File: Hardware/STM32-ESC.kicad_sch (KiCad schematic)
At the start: 0 parts

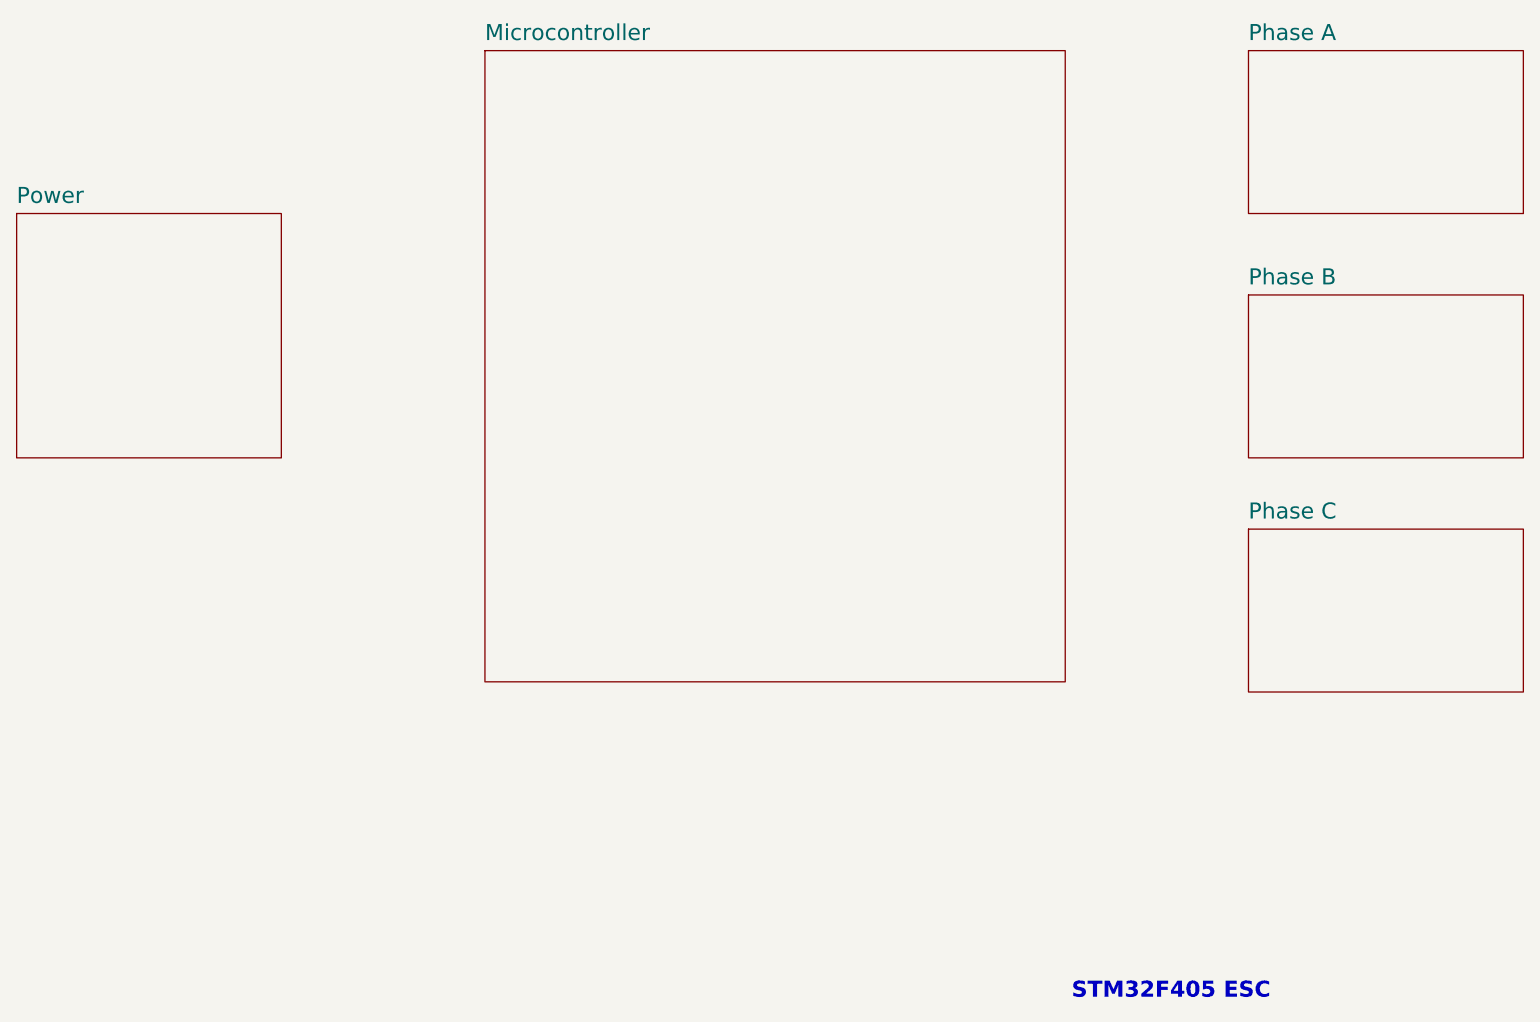
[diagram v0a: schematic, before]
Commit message: feat: Update to use I2C stemma connector
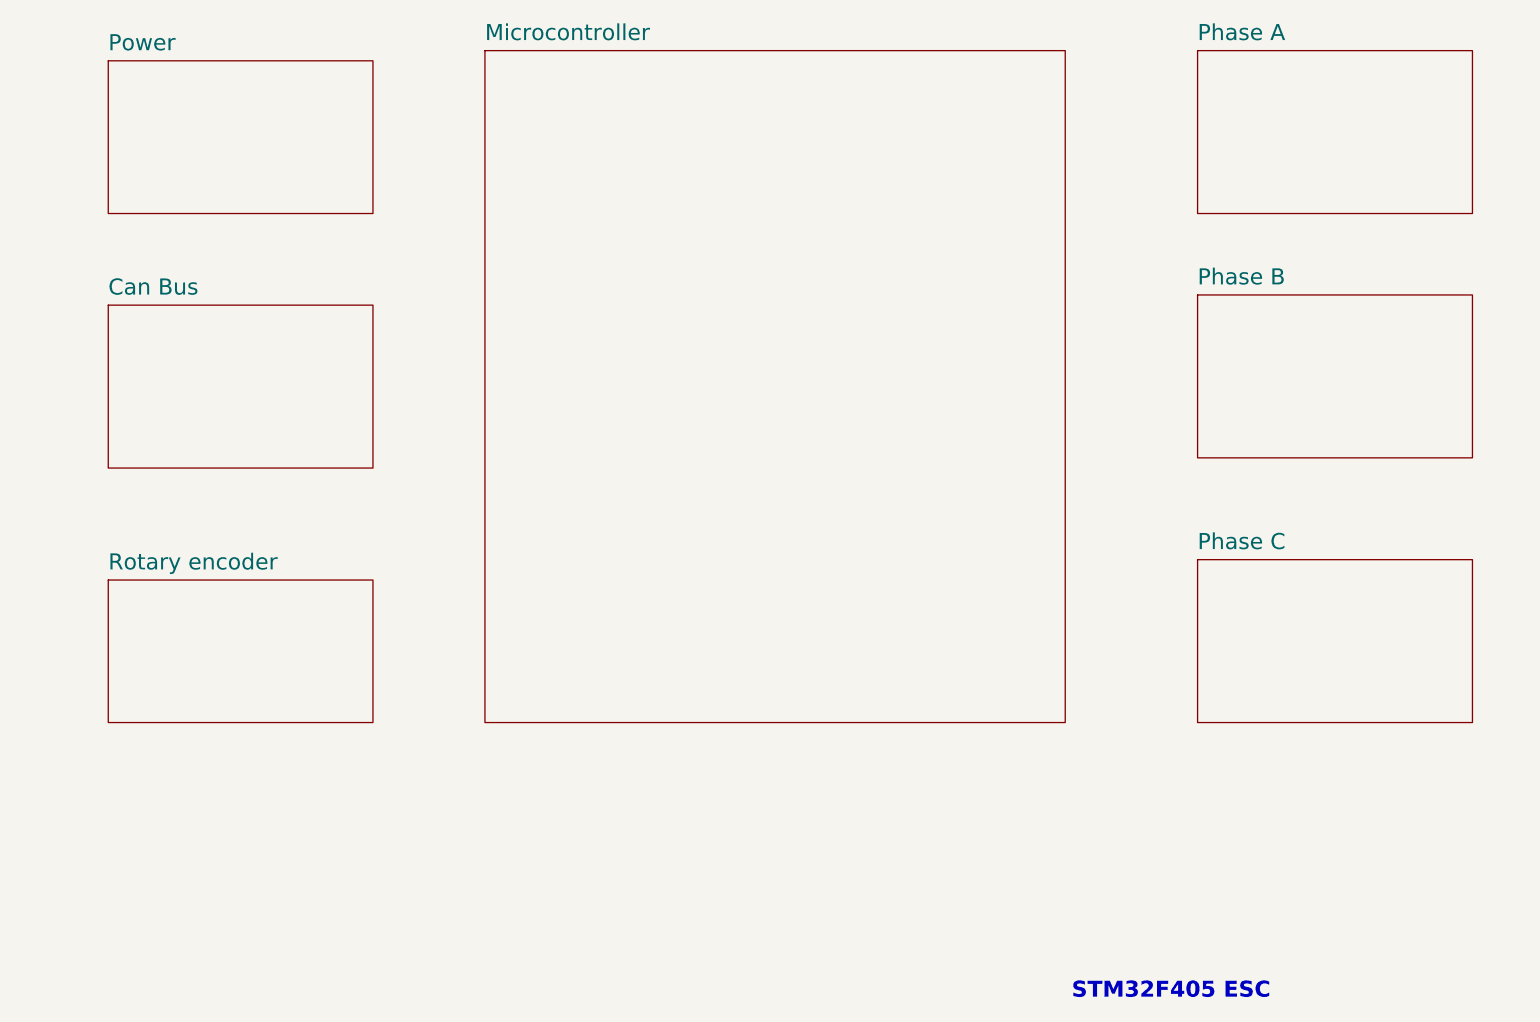
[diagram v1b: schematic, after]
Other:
- added sheet Can Bus (can_bus.kicad_sch)
- added sheet Rotary encoder (rotary_encoder.kicad_sch)
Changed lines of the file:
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@@
 	)
 	(sheet
-		(at 200.66 55.88)
+		(at 194.31 55.88)
 		(size 34.29 20.32)
 		(exclude_from_sim no)
@@
 		)
 		(property "Sheetname" "Phase A"
-			(at 200.66 54.8034 0)
+			(at 194.31 54.8034 0)
 			(effects
 				(font
@@
 		)
 		(property "Sheetfile" "3_phase_A.kicad_sch"
-			(at 200.66 76.7846 0)
+			(at 194.31 76.7846 0)
 			(effects
 				(font
@@
 	)
 	(sheet
-		(at 200.66 115.57)
+		(at 58.42 121.92)
+		(size 33.02 17.78)
+		(exclude_from_sim no)
+		(in_bom yes)
+		(on_board yes)
+		(dnp no)
+		(fields_autoplaced yes)
+		(stroke
+			(width 0.1524)
+			(type solid)
+		)
+		(fill
+			(color 0 0 0 0.0000)
+		)
+		(property "Sheetname" "Rotary encoder"
+			(at 58.42 120.8434 0)
+			(effects
+				(font
+					(size 2 2)
+				)
+				(justify left bottom)
+			)
+		)
+		(property "Sheetfile" "rotary_encoder.kicad_sch"
+			(at 58.42 140.2846 0)
+			(effects
+				(font
+					(size 1.27 1.27)
+				)
+				(justify left top)
+				(hide yes)
+			)
+		)
+		(instances
+			(project "STM32-ESC"
+				(path "/2a01873c-957a-4ca2-97b2-51cbc5d7526f"
+					(page "8")
+				)
+			)
+		)
+	)
+	(sheet
+		(at 194.31 119.38)
 		(size 34.29 20.32)
 		(exclude_from_sim no)
@@
 		)
 		(property "Sheetname" "Phase C"
-			(at 200.66 114.4934 0)
+			(at 194.31 118.3034 0)
 			(effects
 				(font
@@
 		)
 		(property "Sheetfile" "5_phase_C.kicad_sch"
-			(at 200.66 136.4746 0)
+			(at 194.31 140.2846 0)
 			(effects
 				(font
@@
 	)
 	(sheet
-		(at 46.99 76.2)
-		(size 33.02 30.48)
+		(at 58.42 57.15)
+		(size 33.02 19.05)
 		(exclude_from_sim no)
 		(in_bom yes)
@@
 		)
 		(property "Sheetname" "Power"
-			(at 46.99 75.1234 0)
+			(at 58.42 56.0734 0)
 			(effects
 				(font
@@
 		)
 		(property "Sheetfile" "1_power.kicad_sch"
-			(at 46.99 107.2646 0)
+			(at 58.42 76.7846 0)
 			(effects
 				(font
@@
 	(sheet
 		(at 105.41 55.88)
-		(size 72.39 78.74)
+		(size 72.39 83.82)
 		(exclude_from_sim no)
 		(in_bom yes)
@@
 		)
 		(property "Sheetfile" "2_microcontroller.kicad_sch"
-			(at 105.41 135.2046 0)
+			(at 105.41 140.2846 0)
 			(effects
 				(font
@@
 	)
 	(sheet
-		(at 200.66 86.36)
+		(at 58.42 87.63)
+		(size 33.02 20.32)
+		(exclude_from_sim no)
+		(in_bom yes)
+		(on_board yes)
+		(dnp no)
+		(fields_autoplaced yes)
+		(stroke
+			(width 0.1524)
+			(type solid)
+		)
+		(fill
+			(color 0 0 0 0.0000)
+		)
+		(property "Sheetname" "Can Bus"
+			(at 58.42 86.5534 0)
+			(effects
+				(font
+					(size 2 2)
+				)
+				(justify left bottom)
+			)
+		)
+		(property "Sheetfile" "can_bus.kicad_sch"
+			(at 58.42 108.5346 0)
+			(effects
+				(font
+					(size 1.27 1.27)
+				)
+				(justify left top)
+				(hide yes)
+			)
+		)
+		(instances
+			(project "STM32-ESC"
+				(path "/2a01873c-957a-4ca2-97b2-51cbc5d7526f"
+					(page "7")
+				)
+			)
+		)
+	)
+	(sheet
+		(at 194.31 86.36)
 		(size 34.29 20.32)
 		(exclude_from_sim no)
@@
 		)
 		(property "Sheetname" "Phase B"
-			(at 200.66 85.2834 0)
+			(at 194.31 85.2834 0)
 			(effects
 				(font
@@
 		)
 		(property "Sheetfile" "4_phase_B.kicad_sch"
-			(at 200.66 107.2646 0)
-			(effects
-				(font
+			(at 194.31 107.2646 0)
+			(effects
+				(font
